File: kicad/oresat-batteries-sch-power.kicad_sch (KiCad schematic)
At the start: 86 parts, among them J2 SAMTEC-FTS-102-01-X-SJ, Q1 MOSFET-PCH-SOT23-6, Q2 PMV45EN, Q3 MOSFET-PCH-SOT23-6, Q4 MOSFET-PCH-SOT23-6, Q44 PMV45EN, Q5 PMV45EN, U1 MAX7310, U2 MIC842LYC5, U3 MIC842LYC5, U4 MAX4211, U5 TPS6211X, U6 TS5A21366DCUR

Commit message: Updating KiCAD import of EAGLE battery card v3.0 and calling it v3.1 because the gerber files will definitely be different and we'll probably implement a few small changes. Reimports, renames, and fixes .gitignore file. Oh and makes the worksheets pretty.
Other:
- note removed: "1.0"
- note removed: "OreSat battery Card - Power"
- title: (none) -> OreSat Battery Card - Power
- moved on the sheet: C1, C2, C3, C4, C5, C6, C7, C8, C9, D1, D2, D3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

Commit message: Kicad import try #3. Now with DXFs from custom EAGLE layers. Schematic worksheets and names updated.
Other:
- title: OreSat Battery Card - Power -> OreSat Battery Card

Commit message: Move main connector to kicad libraries; start updating text size.
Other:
- title: OreSat Battery Card -> OreSat Battery Card - Power
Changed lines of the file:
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@@
   (paper "B")
   (title_block
-    (title "OreSat Battery Card")
+    (title "OreSat Battery Card - Power")
     (date "2023-12-02")
     (rev "3.1")

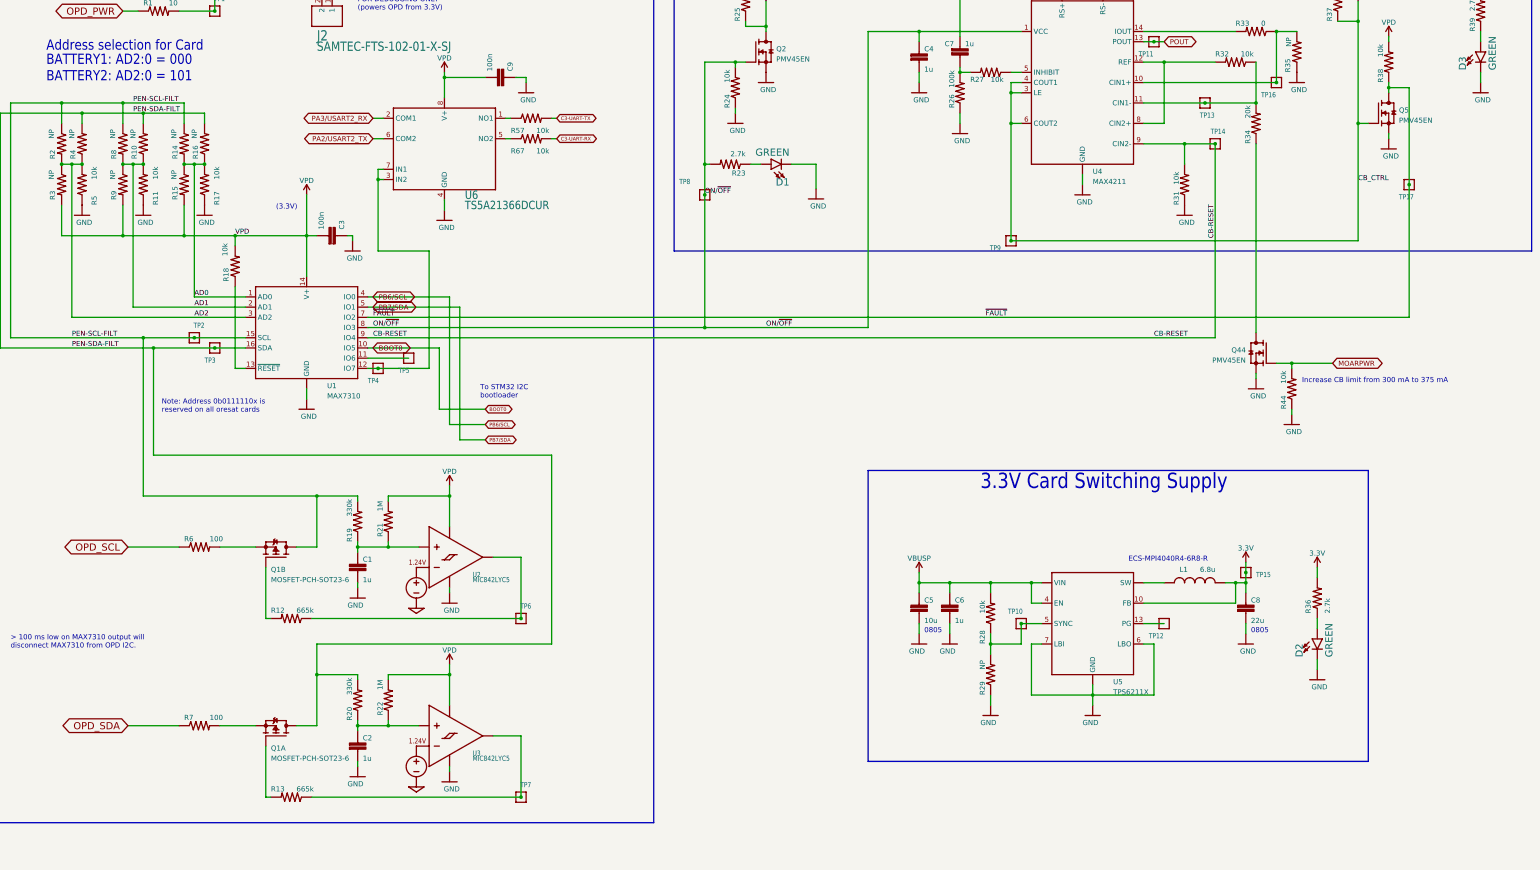
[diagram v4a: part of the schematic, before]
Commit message: Updated ground planes, battery foot prints, zones needs more work.
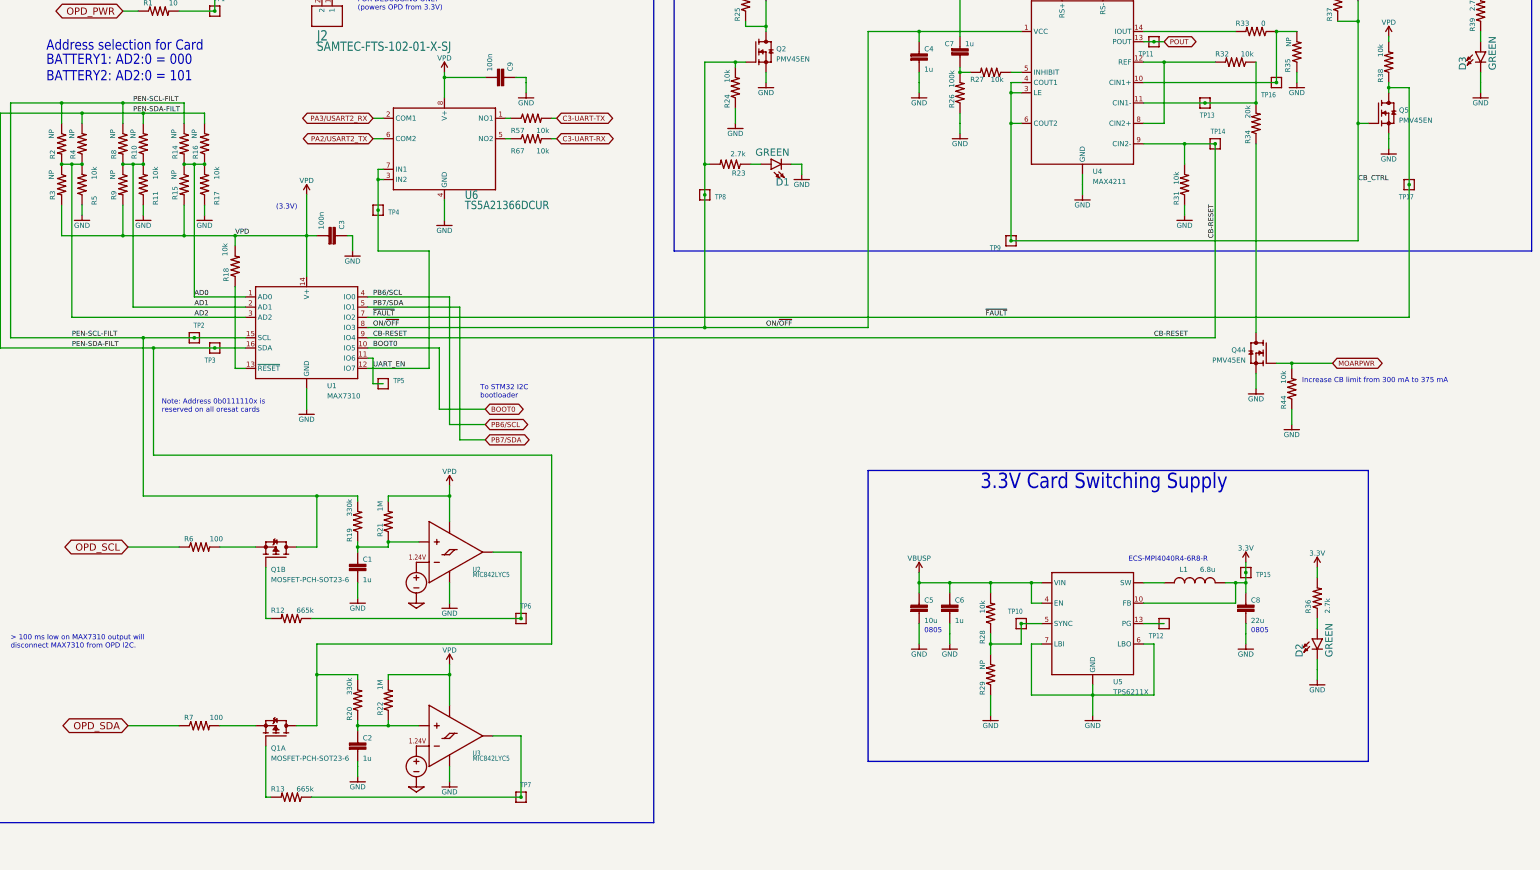
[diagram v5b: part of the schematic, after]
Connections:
- net UART_EN: now reaches TP5.1, U1.11 (IO6)
- net UART_EN: now also TP4.1, U1.12 (IO7), U6.3 (IN2), U6.7 (IN1)
- net PA2/USART2_TX renamed PA2/USART2_TX
- net PA3/USART2_RX renamed PA3/USART2_RX
- net PB6/SCL renamed PB6/SCL
- net PB7/SDA renamed PB7/SDA
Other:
- moved on the sheet: TP4, TP5, U2

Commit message: Starting Battery Card 4.0
Changed root sheet to hierarchical sheet. No change to schematic or layout yet. Updated the stackup with oresat template. Switched to variables for version and date.
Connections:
- net UART_EN: no longer TP5.1, U1.11 (IO6)
- new net: TP5.1, U1.11 (IO6)
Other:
- note added: "ALL CAPS ARE 0603, 10%, X5R or better, AEQ, Vw >= 25 V UNLESS OTHERWISE NOTED ALL RESISTORS ARE 0603 1% AEQ UNLESS OTHERWISE NOTED."
- note removed: "ALL CAPS ARE 0603, 10%, X5R, WV >= 16 V UNLESS OTHERWISE NOTED ALL RESISTORS ARE 0603 1% UNLESS OTHERWISE NOTED"
- company: (none) -> Portland State Aerospace Society
- title: OreSat Battery Card - Power -> OreSat Battery Card

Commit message: Minor polishing, removing outdated OPD signals and OPD power jumper.
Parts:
- removed J2: SAMTEC-FTS-102-01-X-SJ, oresat-batteries:SAMTEC-FTS-102-01-X-S, symbol oresat-batteries-eagle-import:SAMTEC-FTS-102-01-X-SJ
- C5, C8: symbol oresat-batteries-eagle-import:C-EU0805-B-NOSILK -> Device:C_Small
- R10, R14, R15, R16, R2, R3, R4, R8, R9: value NP -> 1K; now not fitted
- R11, R17, R5: value 10k -> 1K
- TP1, TP10, TP11, TP12, TP13, TP14, TP15, TP16, TP17, TP18, TP2, TP3, TP4, TP5, TP6, TP7, TP8, TP9: footprint oresat-batteries:1X01 -> oresat-misc:TestPoint-0.75mm-th; symbol oresat-batteries-eagle-import:TEST-POINT-LARGE-SQUARE -> oresat-misc:Test-Point-0.75mm-th; now left out of the parts list
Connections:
- net PB6/SCL: no longer names the net of U1.4 (IO0)
- net PB7/SDA: no longer names the net of U1.5 (IO1)
- no-connect marks 0 -> 2
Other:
- note removed: "127 mm Jumper FOR DEBUGGING ONLY (powers OPD from 3.3V)"

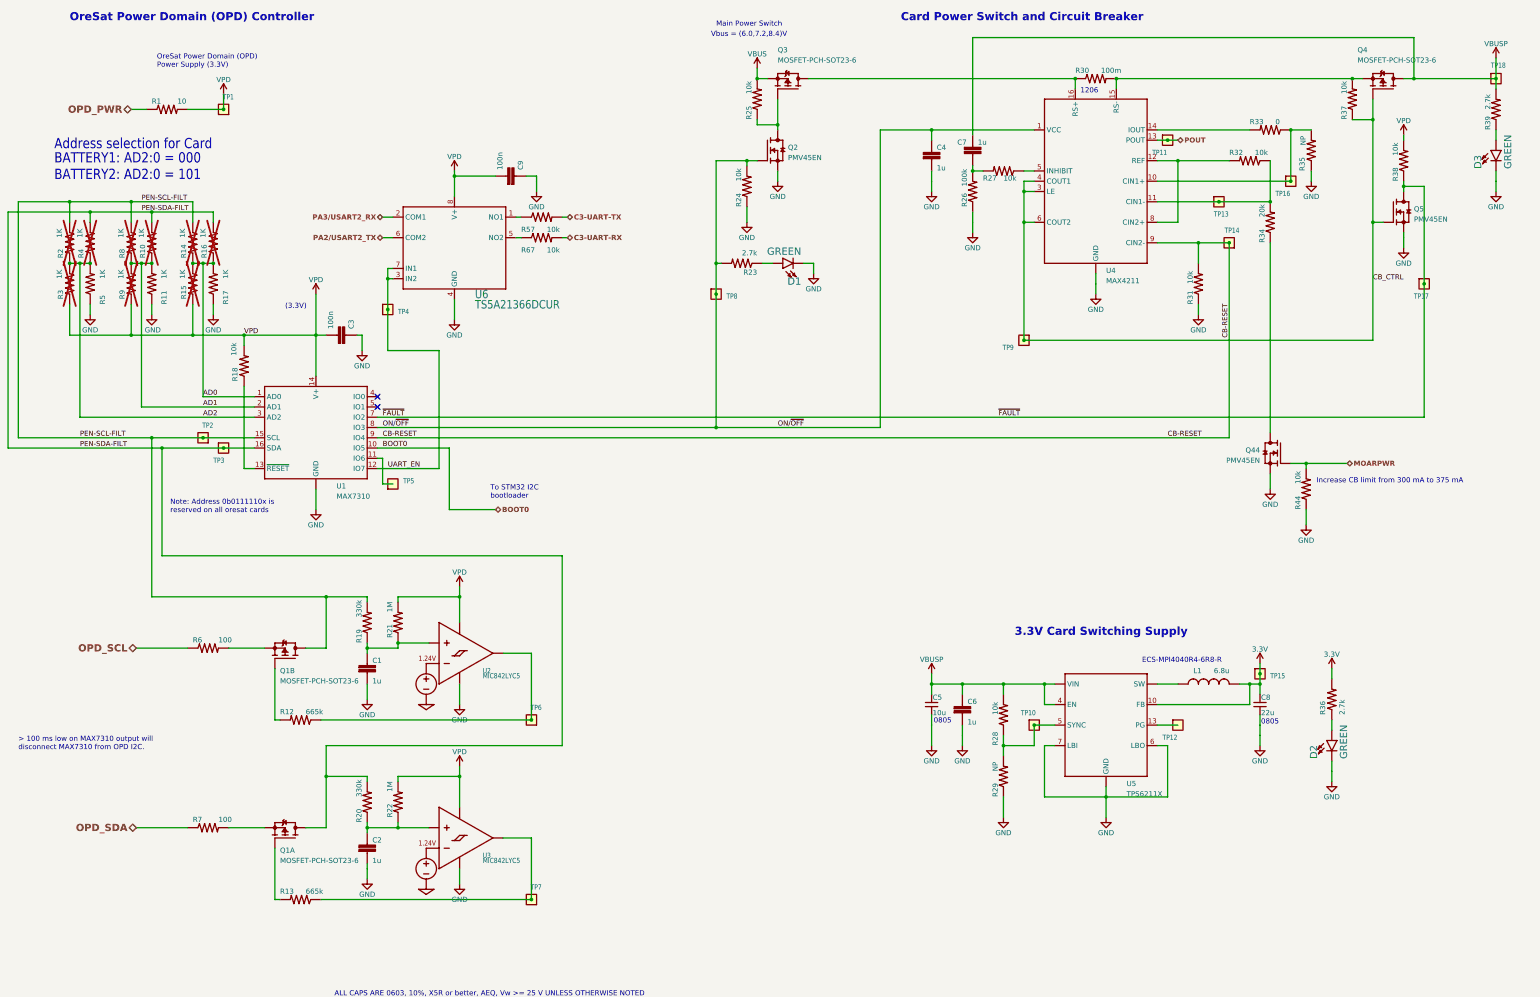
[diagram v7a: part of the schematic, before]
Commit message: Renovated Schematic
Updated schematic symbols and made more uniform with changed resistor, capacitor, and FET symbols. Changed 0603 cap foot print to 0603 small in Oresat passives. Added 2 new resistors and 2 new caps in the power page. Removed old debug connector in favor of the new one. The changes made should make very little updates when pushing the changes to the PCB.
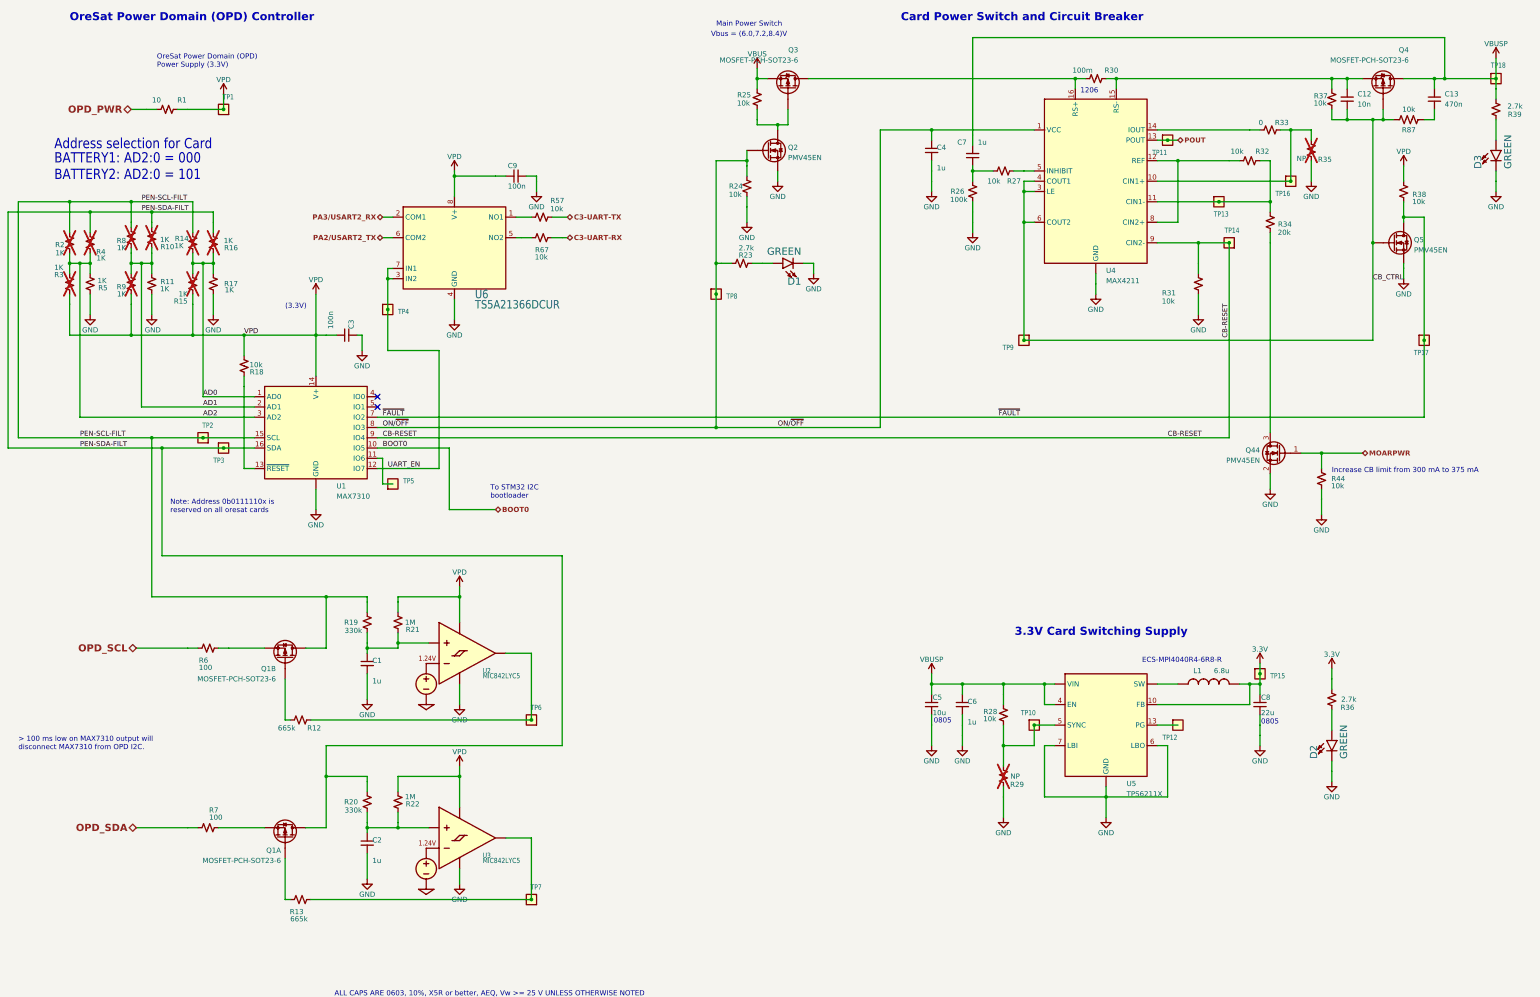
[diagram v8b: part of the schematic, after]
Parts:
- removed Q1: MOSFET-PCH-SOT23-6, oresat-batteries:SOT23-6, symbol oresat-batteries-eagle-import:Q-MOSFET-PCH-dual-SOT23-6_MOSFET-PCH-SOT23-6
- added C12: 10n, oresat-passives:c_0603-SMALL, symbol Device:C_Small
- added C13: 470n, oresat-passives:c_0603-SMALL, symbol Device:C_Small
- added Q1: MOSFET-PCH-SOT23-6, oresat-batteries:SOT23-6, symbol Transistor_FET:Q_Dual_PMOS_G1S2G2D2S1D1
- added R87: 10k, oresat-passives:0603-C-NOSILK, symbol Device:R_US
- C1, C2, C3, C4, C6, C7, C9: footprint oresat-batteries:.0603-C-NOSILK -> oresat-passives:c_0603-SMALL; symbol oresat-batteries-eagle-import:C-EU0603-C-NOSILK -> Device:C_Small
- C5, C8: footprint oresat-batteries:.0805-B-NOSILK -> oresat-passives:0805-B-NOSILK
- Q2, Q44, Q5: symbol oresat-batteries-eagle-import:N-MOSFET-SOT-23-3 -> Transistor_FET:Q_NMOS_GSD
- Q3, Q4: footprint oresat-batteries:SOT23-6 -> Package_TO_SOT_SMD:TSOT-23-6; symbol oresat-batteries-eagle-import:MOSFET-PCH-SOT23-6 -> oresat-transistors:DMP3050LVT-7
- R1, R10, R11, R12, R13, R14, R15, R16, R17, R18, R19, R2, R20, R21, R22, R23, R24, R25, R26, R27, R28, R3, R31, R32, R33, R34, R36, R37, R38, R39, R4, R44, R5, R57, R6, R67, R7, R8, R9: symbol oresat-batteries-eagle-import:R-US_0603-C-NOSILK -> Device:R_Small_US
- R29, R35: symbol oresat-batteries-eagle-import:R-US_0603-C-NOSILK -> Device:R_Small_US; now not fitted
- R30: symbol oresat-batteries-eagle-import:R-US_1206-C -> Device:R_Small_US
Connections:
- net AD2: now also R3.2; no longer R3.1
- net CB_CTRL: now also C12.2, R87.2
- net PEN-SCL-FILT: now also Q1.4 (D)
- net PEN-SDA-FILT: now also Q1.6 (D)
- net VBUSP: now also C13.1
- net VPD: now also R3.1; no longer R3.2
- net at R13.2: now also Q1.1 (G)
- net at R7.2: now also Q1.5 (S)
- net at Q4.4 (S), R30.2, R37.2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: now also C12.1
- net at R6.2: now also Q1.2 (S)
- net at R12.2: now also Q1.3 (G)
- new net: C13.2, R87.1
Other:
- moved on the sheet: TP17
